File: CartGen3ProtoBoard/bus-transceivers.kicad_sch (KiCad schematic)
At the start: 10 parts

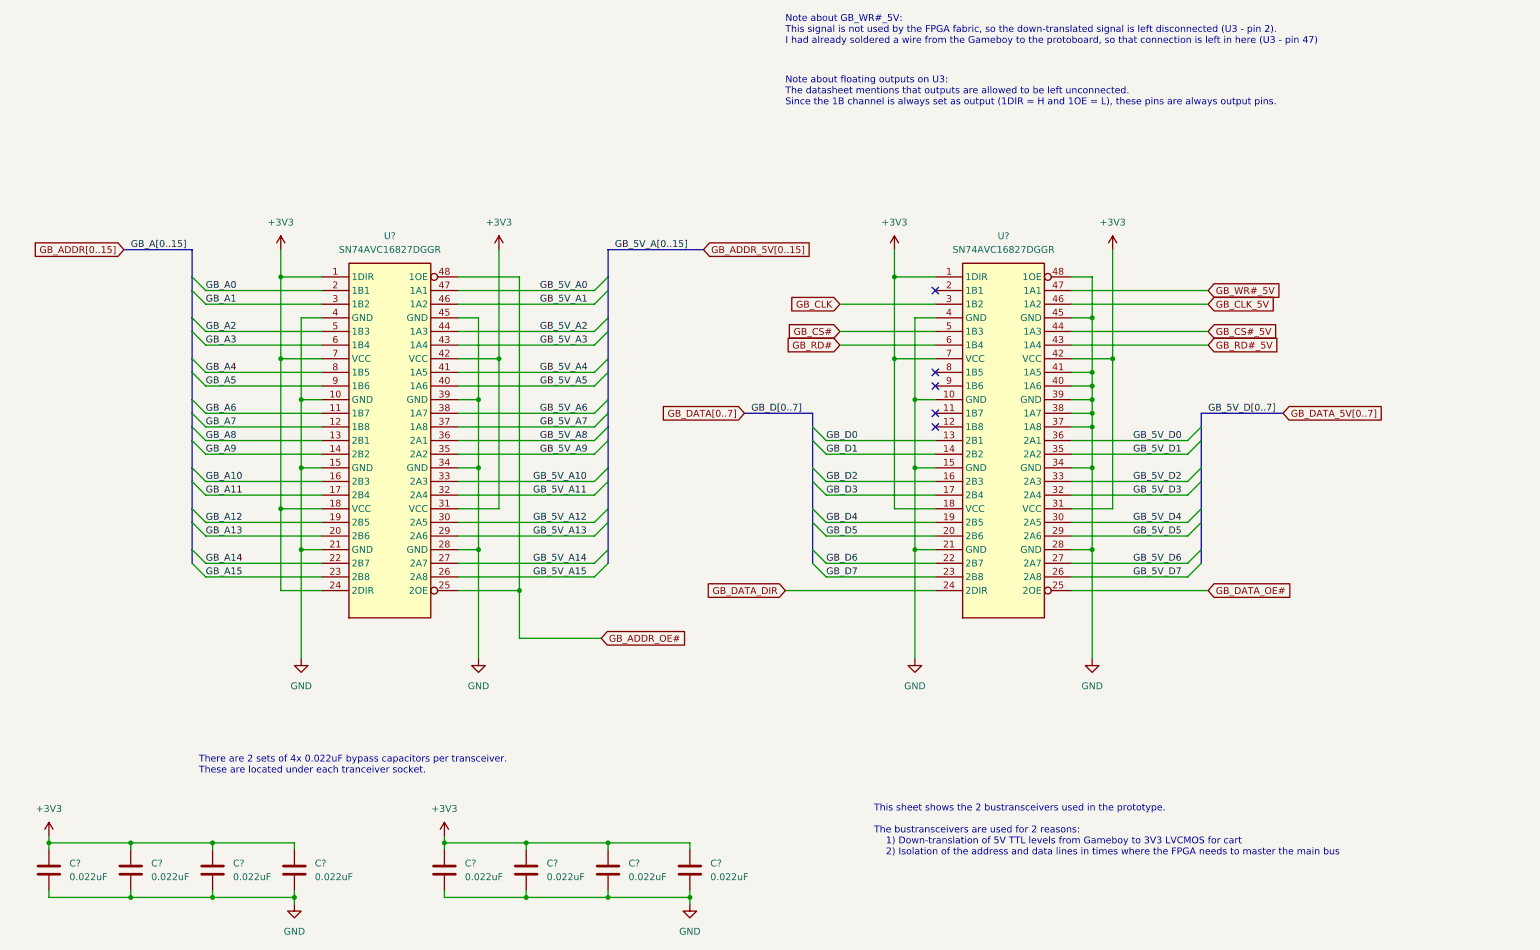
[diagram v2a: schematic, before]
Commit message: Added audio_mixer schematic
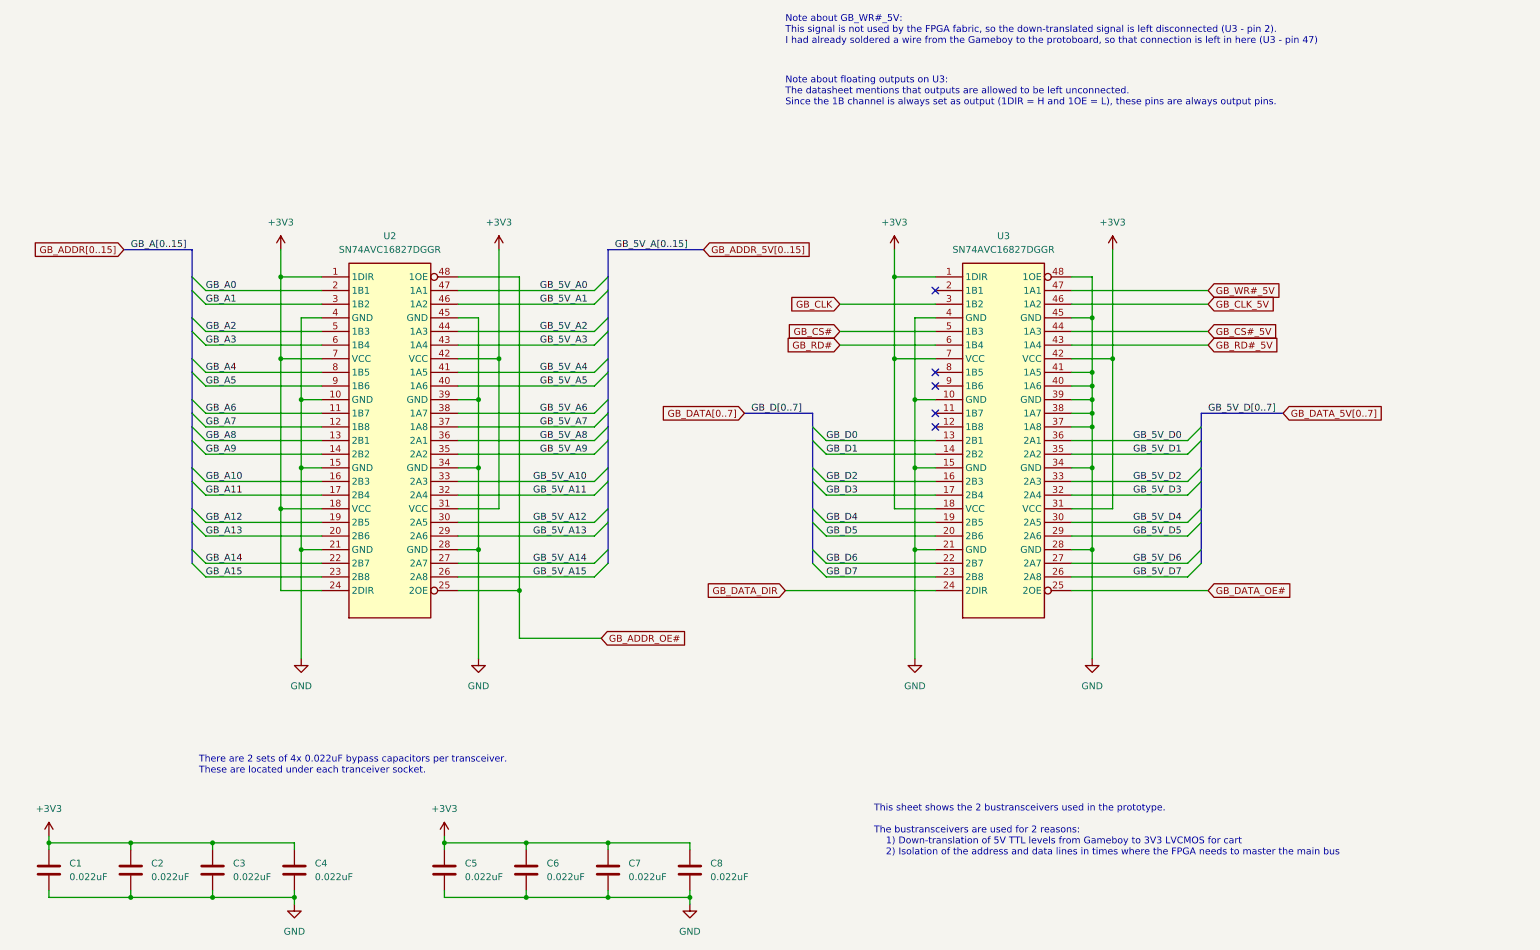
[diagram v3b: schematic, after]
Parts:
- gave numbers to parts that had none: 10
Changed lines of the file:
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@@
     )
   )
-  (symbol (lib_id "Device:C") (at 114.3 180.34 0)
-    (in_bom yes) (on_board yes) (fields_autoplaced)
-    (property "Reference" "C?" (id 0) (at 118.11 179.0699 0)
+  (symbol (lib_id "Device:C") (at 114.3 180.34 0) (unit 1)
+    (in_bom yes) (on_board yes) (fields_autoplaced)
+    (property "Reference" "C6" (id 0) (at 118.11 179.0699 0)
       (effects (font (size 1.27 1.27)) (justify left))
     )
@@
     (pin "2")
   )
-  (symbol (lib_id "Device:C") (at 40.64 180.34 0)
-    (in_bom yes) (on_board yes) (fields_autoplaced)
-    (property "Reference" "C?" (id 0) (at 44.45 179.0699 0)
+  (symbol (lib_id "Device:C") (at 40.64 180.34 0) (unit 1)
+    (in_bom yes) (on_board yes) (fields_autoplaced)
+    (property "Reference" "C2" (id 0) (at 44.45 179.0699 0)
       (effects (font (size 1.27 1.27)) (justify left))
     )
@@
     (pin "2")
   )
-  (symbol (lib_id "power:+3V3") (at 223.52 64.77 0)
-    (in_bom yes) (on_board yes) (fields_autoplaced)
-    (property "Reference" "#PWR?" (id 0) (at 223.52 68.58 0)
+  (symbol (lib_id "power:+3V3") (at 223.52 64.77 0) (unit 1)
+    (in_bom yes) (on_board yes) (fields_autoplaced)
+    (property "Reference" "#PWR0113" (id 0) (at 223.52 68.58 0)
       (effects (font (size 1.27 1.27)) hide)
     )
@@
     (pin "1")
   )
-  (symbol (lib_id "power:+3V3") (at 99.06 173.99 0)
-    (in_bom yes) (on_board yes) (fields_autoplaced)
-    (property "Reference" "#PWR?" (id 0) (at 99.06 177.8 0)
+  (symbol (lib_id "power:+3V3") (at 99.06 173.99 0) (unit 1)
+    (in_bom yes) (on_board yes) (fields_autoplaced)
+    (property "Reference" "#PWR04" (id 0) (at 99.06 177.8 0)
       (effects (font (size 1.27 1.27)) hide)
     )
@@
     (pin "1")
   )
-  (symbol (lib_id "Device:C") (at 129.54 180.34 0)
-    (in_bom yes) (on_board yes) (fields_autoplaced)
-    (property "Reference" "C?" (id 0) (at 133.35 179.0699 0)
+  (symbol (lib_id "Device:C") (at 129.54 180.34 0) (unit 1)
+    (in_bom yes) (on_board yes) (fields_autoplaced)
+    (property "Reference" "C7" (id 0) (at 133.35 179.0699 0)
       (effects (font (size 1.27 1.27)) (justify left))
     )
@@
     (pin "2")
   )
-  (symbol (lib_id "Device:C") (at 144.78 180.34 0)
-    (in_bom yes) (on_board yes) (fields_autoplaced)
-    (property "Reference" "C?" (id 0) (at 148.59 179.0699 0)
+  (symbol (lib_id "Device:C") (at 144.78 180.34 0) (unit 1)
+    (in_bom yes) (on_board yes) (fields_autoplaced)
+    (property "Reference" "C8" (id 0) (at 148.59 179.0699 0)
       (effects (font (size 1.27 1.27)) (justify left))
     )
@@
     (pin "2")
   )
-  (symbol (lib_name "SN74AVC16827DGGR_1") (lib_id "74xx:SN74AVC16827DGGR") (at 88.9 100.33 0)
-    (in_bom yes) (on_board yes) (fields_autoplaced)
-    (property "Reference" "U?" (id 0) (at 88.9 62.23 0))
+  (symbol (lib_name "SN74AVC16827DGGR_1") (lib_id "74xx:SN74AVC16827DGGR") (at 88.9 100.33 0) (unit 1)
+    (in_bom yes) (on_board yes) (fields_autoplaced)
+    (property "Reference" "U2" (id 0) (at 88.9 62.23 0))
     (property "Value" "SN74AVC16827DGGR" (id 1) (at 88.9 64.77 0))
     (property "Footprint" "" (id 2) (at 58.42 134.62 0)
@@
     (pin "9")
   )
-  (symbol (lib_id "Device:C") (at 55.88 180.34 0)
-    (in_bom yes) (on_board yes) (fields_autoplaced)
-    (property "Reference" "C?" (id 0) (at 59.69 179.0699 0)
+  (symbol (lib_id "Device:C") (at 55.88 180.34 0) (unit 1)
+    (in_bom yes) (on_board yes) (fields_autoplaced)
+    (property "Reference" "C3" (id 0) (at 59.69 179.0699 0)
       (effects (font (size 1.27 1.27)) (justify left))
     )
@@
     (pin "2")
   )
-  (symbol (lib_id "power:+3V3") (at 109.22 64.77 0)
-    (in_bom yes) (on_board yes) (fields_autoplaced)
-    (property "Reference" "#PWR?" (id 0) (at 109.22 68.58 0)
+  (symbol (lib_id "power:+3V3") (at 109.22 64.77 0) (unit 1)
+    (in_bom yes) (on_board yes) (fields_autoplaced)
+    (property "Reference" "#PWR0110" (id 0) (at 109.22 68.58 0)
       (effects (font (size 1.27 1.27)) hide)
     )
@@
     (pin "1")
   )
-  (symbol (lib_id "power:GND") (at 219.71 140.97 0)
-    (in_bom yes) (on_board yes) (fields_autoplaced)
-    (property "Reference" "#PWR?" (id 0) (at 219.71 147.32 0)
+  (symbol (lib_id "power:GND") (at 219.71 140.97 0) (unit 1)
+    (in_bom yes) (on_board yes) (fields_autoplaced)
+    (property "Reference" "#PWR0111" (id 0) (at 219.71 147.32 0)
       (effects (font (size 1.27 1.27)) hide)
     )
@@
     (pin "1")
   )
-  (symbol (lib_id "power:GND") (at 72.39 140.97 0)
-    (in_bom yes) (on_board yes) (fields_autoplaced)
-    (property "Reference" "#PWR?" (id 0) (at 72.39 147.32 0)
+  (symbol (lib_id "power:GND") (at 72.39 140.97 0) (unit 1)
+    (in_bom yes) (on_board yes) (fields_autoplaced)
+    (property "Reference" "#PWR0109" (id 0) (at 72.39 147.32 0)
       (effects (font (size 1.27 1.27)) hide)
     )
@@
     (pin "1")
   )
-  (symbol (lib_id "power:+3V3") (at 25.4 173.99 0)
-    (in_bom yes) (on_board yes) (fields_autoplaced)
-    (property "Reference" "#PWR?" (id 0) (at 25.4 177.8 0)
+  (symbol (lib_id "power:+3V3") (at 25.4 173.99 0) (unit 1)
+    (in_bom yes) (on_board yes) (fields_autoplaced)
+    (property "Reference" "#PWR02" (id 0) (at 25.4 177.8 0)
       (effects (font (size 1.27 1.27)) hide)
     )
@@
     (pin "1")
   )
-  (symbol (lib_id "power:GND") (at 71.12 186.69 0)
-    (in_bom yes) (on_board yes) (fields_autoplaced)
-    (property "Reference" "#PWR?" (id 0) (at 71.12 193.04 0)
+  (symbol (lib_id "power:GND") (at 71.12 186.69 0) (unit 1)
+    (in_bom yes) (on_board yes) (fields_autoplaced)
+    (property "Reference" "#PWR03" (id 0) (at 71.12 193.04 0)
       (effects (font (size 1.27 1.27)) hide)
     )
@@
     (pin "1")
   )
-  (symbol (lib_id "power:GND") (at 186.69 140.97 0)
-    (in_bom yes) (on_board yes) (fields_autoplaced)
-    (property "Reference" "#PWR?" (id 0) (at 186.69 147.32 0)
+  (symbol (lib_id "power:GND") (at 186.69 140.97 0) (unit 1)
+    (in_bom yes) (on_board yes) (fields_autoplaced)
+    (property "Reference" "#PWR0112" (id 0) (at 186.69 147.32 0)
       (effects (font (size 1.27 1.27)) hide)
     )
@@
     (pin "1")
   )
-  (symbol (lib_id "Device:C") (at 71.12 180.34 0)
-    (in_bom yes) (on_board yes) (fields_autoplaced)
-    (property "Reference" "C?" (id 0) (at 74.93 179.0699 0)
+  (symbol (lib_id "Device:C") (at 71.12 180.34 0) (unit 1)
+    (in_bom yes) (on_board yes) (fields_autoplaced)
+    (property "Reference" "C4" (id 0) (at 74.93 179.0699 0)
       (effects (font (size 1.27 1.27)) (justify left))
     )
@@
     (pin "2")
   )
-  (symbol (lib_id "power:+3V3") (at 182.88 64.77 0)
-    (in_bom yes) (on_board yes) (fields_autoplaced)
-    (property "Reference" "#PWR?" (id 0) (at 182.88 68.58 0)
+  (symbol (lib_id "power:+3V3") (at 182.88 64.77 0) (unit 1)
+    (in_bom yes) (on_board yes) (fields_autoplaced)
+    (property "Reference" "#PWR0114" (id 0) (at 182.88 68.58 0)
       (effects (font (size 1.27 1.27)) hide)
     )
@@
     (pin "1")
   )
-  (symbol (lib_id "Device:C") (at 25.4 180.34 0)
-    (in_bom yes) (on_board yes) (fields_autoplaced)
-    (property "Reference" "C?" (id 0) (at 29.21 179.0699 0)
+  (symbol (lib_id "Device:C") (at 25.4 180.34 0) (unit 1)
+    (in_bom yes) (on_board yes) (fields_autoplaced)
+    (property "Reference" "C1" (id 0) (at 29.21 179.0699 0)
       (effects (font (size 1.27 1.27)) (justify left))
     )
@@
     (pin "2")
   )
-  (symbol (lib_id "power:GND") (at 105.41 140.97 0)
-    (in_bom yes) (on_board yes) (fields_autoplaced)
-    (property "Reference" "#PWR?" (id 0) (at 105.41 147.32 0)
+  (symbol (lib_id "power:GND") (at 105.41 140.97 0) (unit 1)
+    (in_bom yes) (on_board yes) (fields_autoplaced)
+    (property "Reference" "#PWR0108" (id 0) (at 105.41 147.32 0)
       (effects (font (size 1.27 1.27)) hide)
     )
@@
     (pin "1")
   )
-  (symbol (lib_id "74xx:SN74AVC16827DGGR") (at 203.2 100.33 0)
-    (in_bom yes) (on_board yes) (fields_autoplaced)
-    (property "Reference" "U?" (id 0) (at 203.2 62.23 0))
+  (symbol (lib_id "74xx:SN74AVC16827DGGR") (at 203.2 100.33 0) (unit 1)
+    (in_bom yes) (on_board yes) (fields_autoplaced)
+    (property "Reference" "U3" (id 0) (at 203.2 62.23 0))
     (property "Value" "SN74AVC16827DGGR" (id 1) (at 203.2 64.77 0))
     (property "Footprint" "" (id 2) (at 172.72 134.62 0)
@@
     (pin "9")
   )
-  (symbol (lib_id "Device:C") (at 99.06 180.34 0)
-    (in_bom yes) (on_board yes) (fields_autoplaced)
-    (property "Reference" "C?" (id 0) (at 102.87 179.0699 0)
+  (symbol (lib_id "Device:C") (at 99.06 180.34 0) (unit 1)
+    (in_bom yes) (on_board yes) (fields_autoplaced)
+    (property "Reference" "C5" (id 0) (at 102.87 179.0699 0)
       (effects (font (size 1.27 1.27)) (justify left))
     )
@@
     (pin "2")
   )
-  (symbol (lib_id "power:GND") (at 144.78 186.69 0)
-    (in_bom yes) (on_board yes) (fields_autoplaced)
-    (property "Reference" "#PWR?" (id 0) (at 144.78 193.04 0)
+  (symbol (lib_id "power:GND") (at 144.78 186.69 0) (unit 1)
+    (in_bom yes) (on_board yes) (fields_autoplaced)
+    (property "Reference" "#PWR05" (id 0) (at 144.78 193.04 0)
       (effects (font (size 1.27 1.27)) hide)
     )
@@
     (pin "1")
   )
-  (symbol (lib_id "power:+3V3") (at 68.58 64.77 0)
-    (in_bom yes) (on_board yes) (fields_autoplaced)
-    (property "Reference" "#PWR?" (id 0) (at 68.58 68.58 0)
-      (effects (font (size 1.27 1.27)) hide)
-    )
+  (symbol (lib_id "power:+3V3") (at 68.58 64.77 0) (unit 1)
+    (in_bom yes) (on_board yes) (fields_autoplaced)
+    (property "Reference" "#PWR0107" (id 0) (at 68.58 68.58 0)
+      (effects (font (size 1.27 1.27)) hide)
+    )
